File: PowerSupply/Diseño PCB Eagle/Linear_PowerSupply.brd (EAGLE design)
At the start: 100 x 80 mm, 32 parts, among them SW04 RECTIFIER-RB1A

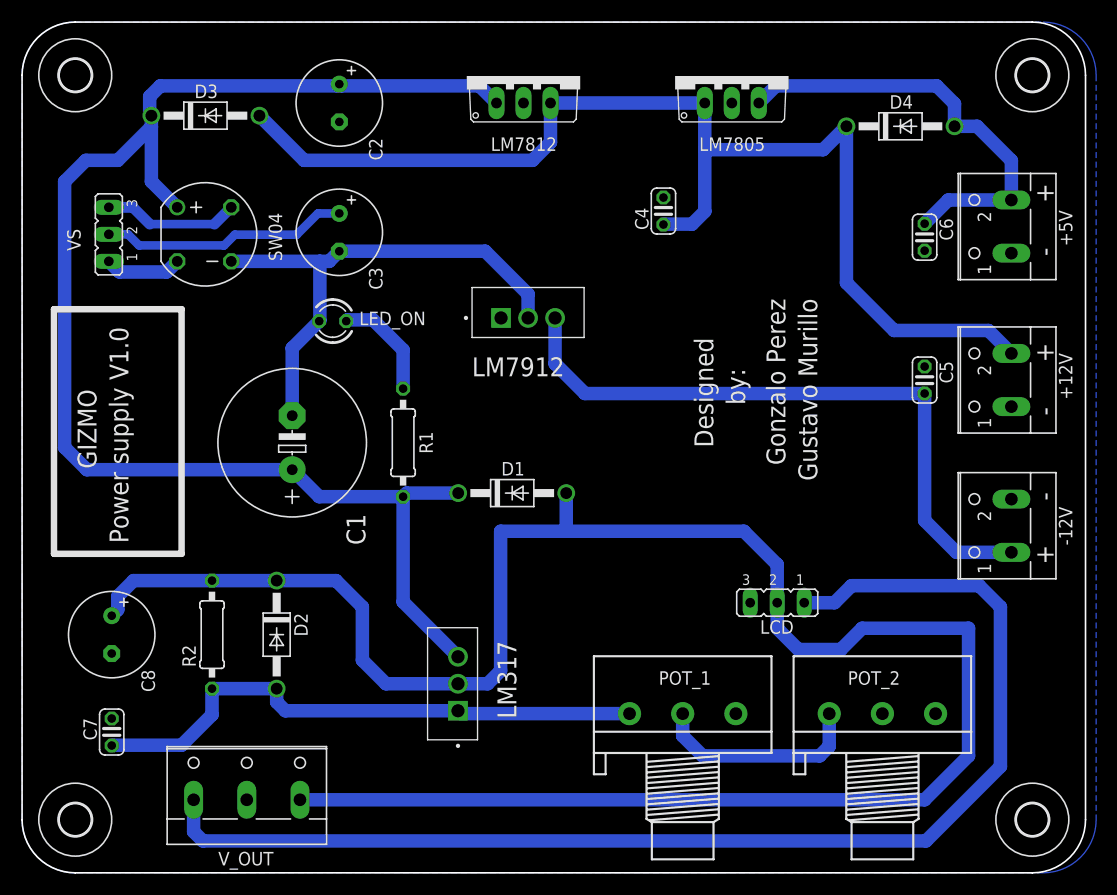
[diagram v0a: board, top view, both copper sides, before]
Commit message: update PCB pads design Se ha actualizado el archivo Eagle correspondiente al diseño de los pads de la tarjeta impresa. Dentro de los cambios se ha aumentado el tamaño de cada terminal. Es importante observar que exist un ligero solapamiento entre los terminales de cada CI, por lo que al maquinar será indispensable contar con una fresa de al menos 1mm para desbastar adecuadamente las uniones. La conexión de la tierra comun a los elementos ha sido modificada al implementar buses curvos.
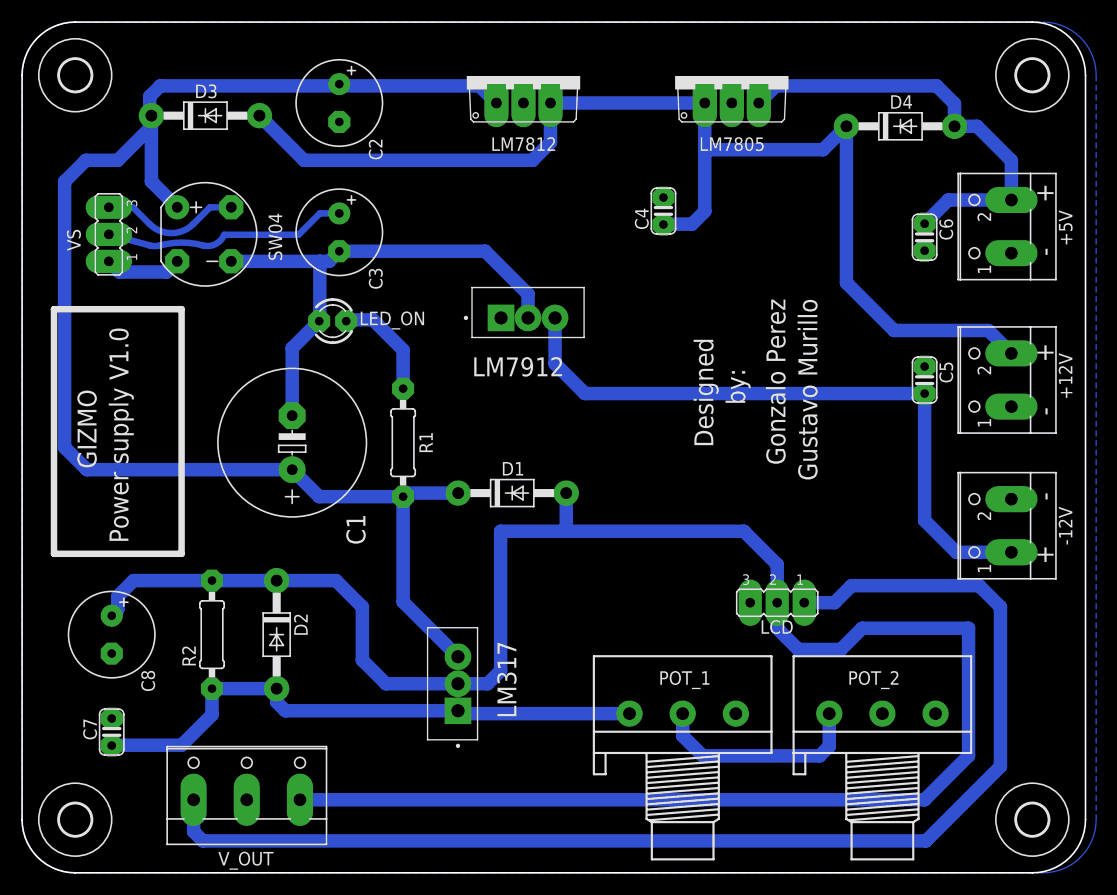
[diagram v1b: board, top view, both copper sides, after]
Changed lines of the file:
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@@
 </layers>
 <board>
-<fusionsync huburn="a.YnVzaW5lc3M6dWd0bzYz" projecturn="a.YnVzaW5lc3M6dWd0bzYzIzIwMjEwOTI3NDQ5MDIyNjU2" f3durn="urn:adsk.wipprod:dm.lineage:OlAsaMdZTC2gfCX6jfuC9w" pcbguid="" lastpulledtime="" lastsyncedchangeguid="" latestrevisionid="1fcd2507-a7d3-4798-8f05-8fcfd777ff43" lastsyncedrevisionid="1fcd2507-a7d3-4798-8f05-8fcfd777ff43" lastboardhashguid="ba02d99f-0dbd-02f6-fa4f-ac9a706960af" lastpushedtime="2021-10-13T16:02:34Z" linktopcb3d="true"/>
+<fusionsync huburn="a.YnVzaW5lc3M6dWd0bzYz" projecturn="a.YnVzaW5lc3M6dWd0bzYzIzIwMjEwOTI3NDQ5MDIyNjU2" f3durn="urn:adsk.wipprod:dm.lineage:OlAsaMdZTC2gfCX6jfuC9w" pcbguid="" lastpulledtime="" lastsyncedchangeguid="" latestrevisionid="1fcd2507-a7d3-4798-8f05-8fcfd777ff43" lastsyncedrevisionid="1fcd2507-a7d3-4798-8f05-8fcfd777ff43" lastboardhashguid="ba02d99f-0dbd-02f6-fa4f-ac9a706960af" lastpushedtime="2021-10-13T16:02:34Z" linktopcb3d="false"/>
 <plain>
 <wire x1="0" y1="75" x2="0" y2="5" width="0.1524" layer="20"/>
@@
 </class>
 </classes>
-<designrules name="default">
+<designrules name="default *">
 <description language="de">&lt;b&gt;EAGLE Design Rules&lt;/b&gt;
 &lt;p&gt;
@@
 <param name="rvMicroViaOuter" value="0.25"/>
 <param name="rvMicroViaInner" value="0.25"/>
-<param name="rlMinPadTop" value="10mil"/>
-<param name="rlMaxPadTop" value="20mil"/>
-<param name="rlMinPadInner" value="10mil"/>
-<param name="rlMaxPadInner" value="20mil"/>
-<param name="rlMinPadBottom" value="10mil"/>
-<param name="rlMaxPadBottom" value="20mil"/>
+<param name="rlMinPadTop" value="25mil"/>
+<param name="rlMaxPadTop" value="40mil"/>
+<param name="rlMinPadInner" value="25mil"/>
+<param name="rlMaxPadInner" value="40mil"/>
+<param name="rlMinPadBottom" value="25mil"/>
+<param name="rlMaxPadBottom" value="40mil"/>
 <param name="rlMinViaOuter" value="8mil"/>
 <param name="rlMaxViaOuter" value="20mil"/>
@@
 <param name="srMinRoundness" value="0mil"/>
 <param name="srMaxRoundness" value="0mil"/>
-<param name="slThermalIsolate" value="10mil"/>
+<param name="slThermalIsolate" value="0mil"/>
 <param name="slThermalsForVias" value="0"/>
 <param name="dpMaxLengthDifference" value="10mm"/>
@@
 <vertex x="101" y="5" curve="-90"/>
 </polygon>
-<wire x1="27.83" y1="62.008" x2="29.83" y2="62.008" width="0.8128" layer="16"/>
-<wire x1="27.83" y1="62.008" x2="25.83" y2="60.008" width="0.8128" layer="16"/>
-<wire x1="25.83" y1="60.008" x2="20.008" y2="60.008" width="0.8128" layer="16"/>
-<wire x1="20.008" y1="60.008" x2="19" y2="59" width="0.8128" layer="16"/>
-<wire x1="9.96" y1="60.04" x2="8.16" y2="60.04" width="0.8128" layer="16"/>
-<wire x1="19" y1="59" x2="11" y2="59" width="0.8128" layer="16"/>
-<wire x1="11" y1="59" x2="9.96" y2="60.04" width="0.8128" layer="16"/>
+<wire x1="8.16" y1="60.04" x2="12" y2="59" width="0.6096" layer="16"/>
+<wire x1="12" y1="59" x2="13" y2="59" width="0.6096" layer="16" curve="30.308147"/>
+<wire x1="13" y1="59" x2="17" y2="59" width="0.6096" layer="16" curve="-30.308209"/>
+<wire x1="17" y1="59" x2="19" y2="60" width="0.6096" layer="16" curve="83.438384"/>
+<wire x1="19" y1="60" x2="26" y2="60" width="0.6096" layer="16"/>
+<wire x1="28.008" y1="62.008" x2="29.83" y2="62.008" width="0.6096" layer="16"/>
+<wire x1="26" y1="60" x2="28.008" y2="62.008" width="0.6096" layer="16"/>
+<wire x1="21.13" y1="6.87" x2="8.43" y2="14.51" width="0" layer="19" extent="1-1"/>
 </signal>
 <signal name="VAC+">
 <contactref element="SW04" pad="AC1"/>
 <contactref element="VS" pad="3"/>
-<wire x1="8.16" y1="62.58" x2="10.42" y2="62.58" width="1.016" layer="16"/>
-<wire x1="18.09" y1="61" x2="19.67" y2="62.58" width="1.016" layer="16"/>
-<wire x1="10.42" y1="62.58" x2="12" y2="61" width="1.016" layer="16"/>
-<wire x1="12" y1="61" x2="18.09" y2="61" width="0.8128" layer="16"/>
+<wire x1="8.16" y1="62.58" x2="10.42" y2="62.58" width="0.6096" layer="16"/>
+<wire x1="17.67" y1="62.58" x2="19.67" y2="62.58" width="0.6096" layer="16"/>
+<wire x1="17.67" y1="62.58" x2="16.09" y2="61" width="0.6096" layer="16"/>
+<wire x1="10.42" y1="62.58" x2="12" y2="61" width="0.6096" layer="16"/>
+<wire x1="12" y1="61" x2="16.09" y2="61" width="0.6096" layer="16" curve="90"/>
 </signal>
 <signal name="VAC-">
@@
 <mfgpreviewcolor name="substratecolor" color="0xFF786E46"/>
 </mfgpreviewcolors>
+<errors>
+</errors>
 </board>
 </drawing>
